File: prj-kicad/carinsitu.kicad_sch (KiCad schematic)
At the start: 52 parts, among them P1 BAT, P2 MOT, P3 CONN_3, P4 CONN_4, SW1 SWITCH_SLIDE, SW2 SW_Push, U1 LoLin_D1_mini_pro, U2 MIC2860, U3 MAX17205, U4 SN74LVC1T45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

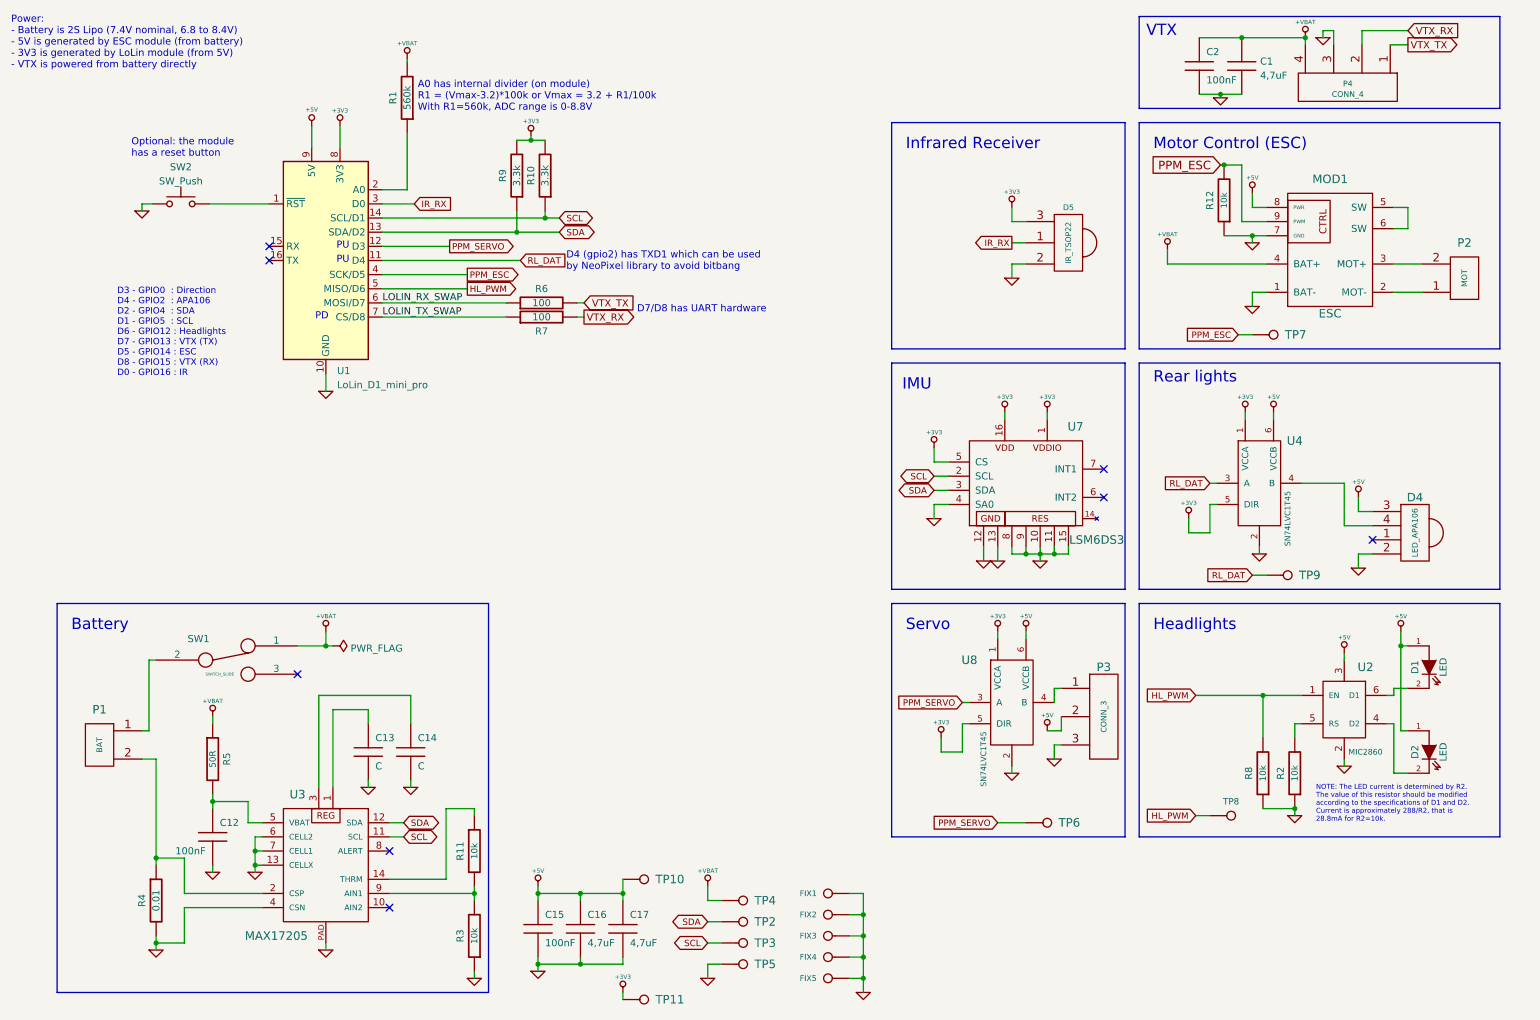
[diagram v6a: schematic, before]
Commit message: Add zero ohm resistors
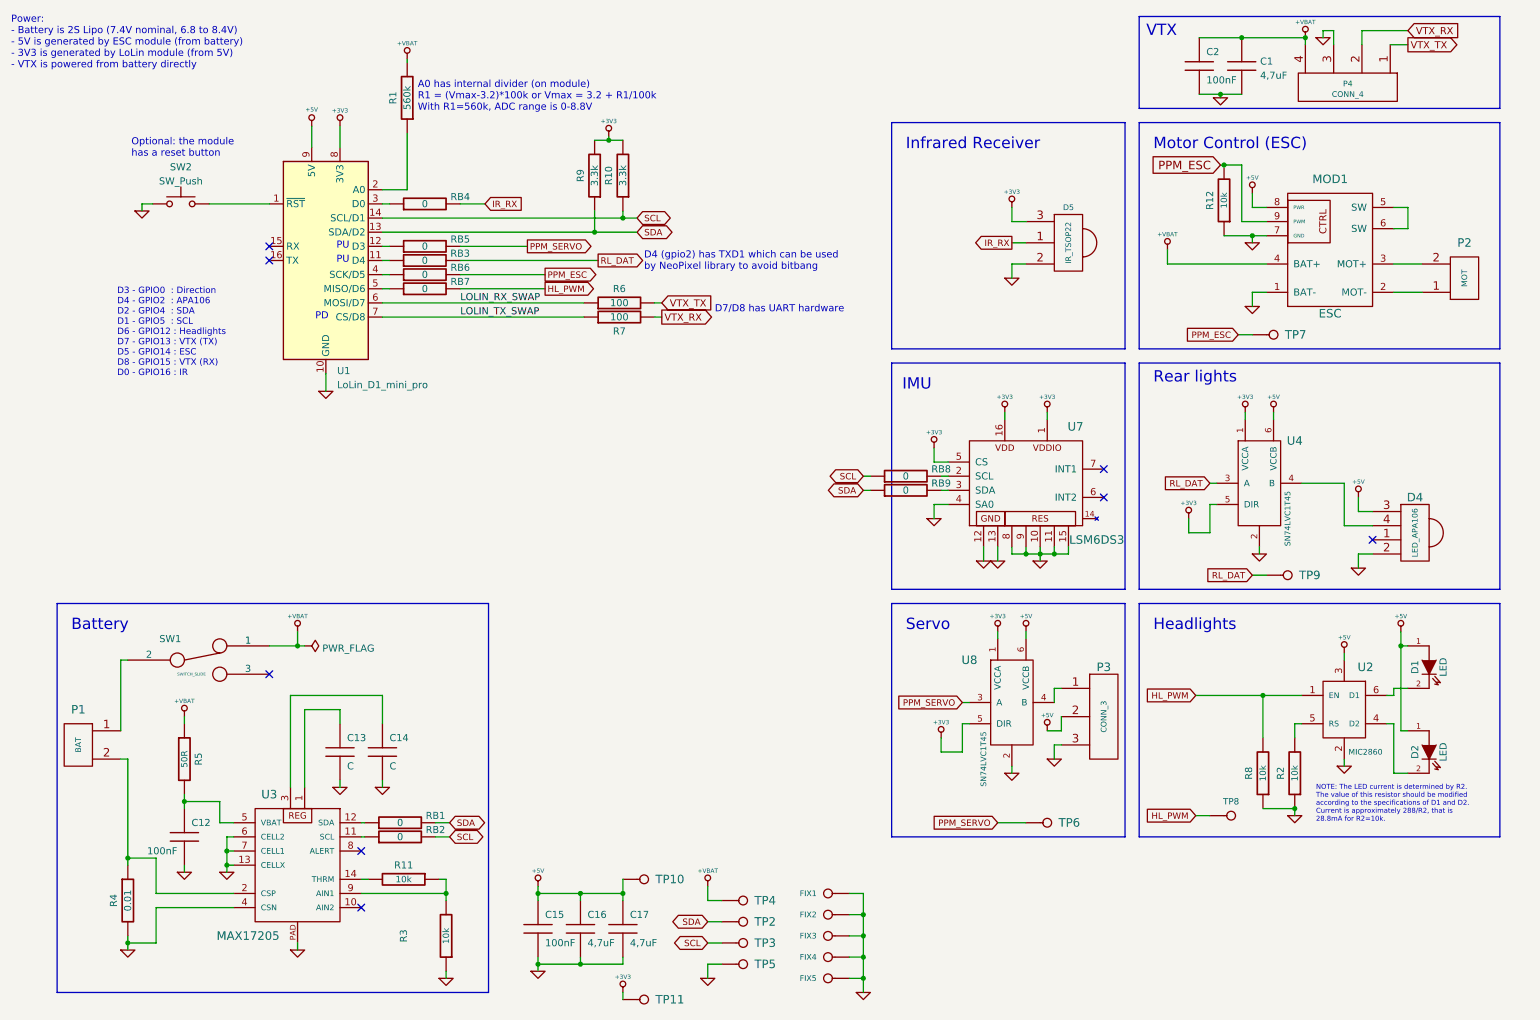
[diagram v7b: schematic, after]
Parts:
- added RB1, RB2, RB3, RB4, RB5, RB6, RB7, RB8, RB9: 0, symbol carinsitu:R
- C1, R1, R10, R6, R7, R9: footprint (none) -> carinsitu:SMD0805
- P4: footprint (none) -> carinsitu:CONN_61300411121
- SW2: footprint (none) -> Button_Switch_SMD:SW_Push_SPST_NO_Alps_SKRK
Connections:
- net HL_PWM: now also RB7.2; no longer U1.5 (MISO/D6)
- net IR_RX: now also RB4.2; no longer U1.3 (D0)
- net PPM_ESC: now also RB6.2; no longer U1.4 (SCK/D5)
- net PPM_SERVO: now also RB5.2; no longer U1.12 (D3)
- net RL_DAT: now also RB3.2; no longer U1.11 (D4)
- net SCL: now also RB2.2, RB8.1; no longer U3.11 (SCL), U7.2 (SCL)
- net SDA: now also RB1.2, RB9.1; no longer U3.12 (SDA), U7.3 (SDA)
- net at R3.2, U3.9 (AIN1): now also R11.1; no longer R11.2
- net at U3.14 (THRM): now also R11.2; no longer R11.1
- new net: RB8.2, U7.2 (SCL)
- new net: RB9.2, U7.3 (SDA)
- new net: RB2.1, U3.11 (SCL)
- new net: RB1.1, U3.12 (SDA)
- new net: RB3.1, U1.11 (D4)
- new net: RB5.1, U1.12 (D3)
- new net: RB4.1, U1.3 (D0)
- new net: RB6.1, U1.4 (SCK/D5)
- new net: RB7.1, U1.5 (MISO/D6)
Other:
- moved on the sheet: C12, C13, C14, P1, R10, R11, R3, R4, R5, R6, R7, R9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

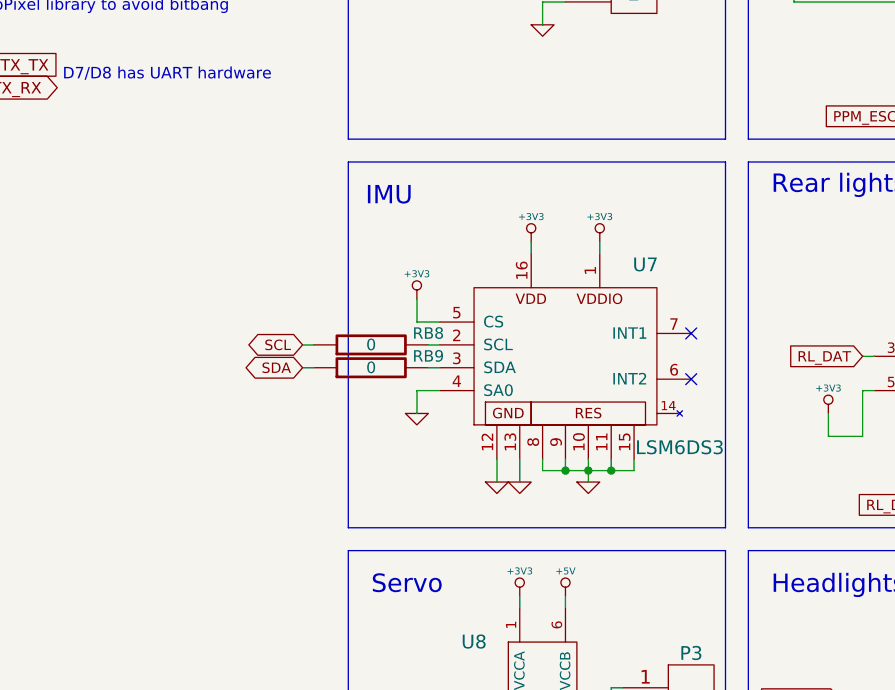
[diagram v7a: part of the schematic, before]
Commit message: Redesign IMU connections
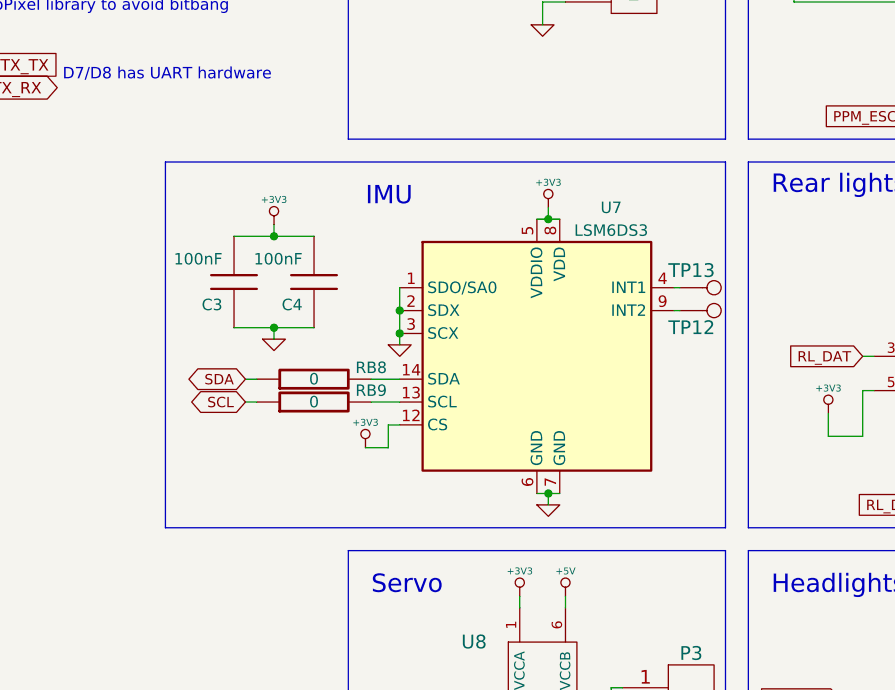
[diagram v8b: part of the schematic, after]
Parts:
- removed U7: LSM6DS3, carinsitu:LGA-16, symbol carinsitu:LSM6D3
- added C3, C4: 100nF, carinsitu:SMD0603, symbol carinsitu:C
- added TP12, TP13: CONN_1, carinsitu:TP, symbol carinsitu:CONN_1
- added U7: LSM6DS3, Package_LGA:LGA-14_3x2.5mm_P0.5mm_LayoutBorder3x4y, symbol Sensor_Motion:LSM6DS3
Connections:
- net +3V3: now also C3.2, C4.2, U7.12 (CS), U7.5 (VDDIO), U7.8 (VDD)
- net GND: now also C3.1, C4.1, U7.1 (SDO/SA0), U7.2 (SDX), U7.3 (SCX), U7.6 (GND), U7.7 (GND)
- net SCL: now also RB9.1; no longer RB8.1
- net SDA: now also RB8.1; no longer RB9.1
- net at RB8.2: now also U7.14 (SDA)
- net at RB9.2: now also U7.13 (SCL)
- new net: TP13.1, U7.4 (INT1)
- new net: TP12.1, U7.9 (INT2)
- no-connect marks 8 -> 6
